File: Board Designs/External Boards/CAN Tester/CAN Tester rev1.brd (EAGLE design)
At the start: 83.8 x 100.3 mm, 27 parts, among them M1 Minifit, M2 Nanofit, M3 Nanofit-1, M4 Minifit-1, U1 ISOLATED CAN TRANSCIEVER, U3 TEENSY_3.2_SIMPLE, U4 CHARACTER_LCD

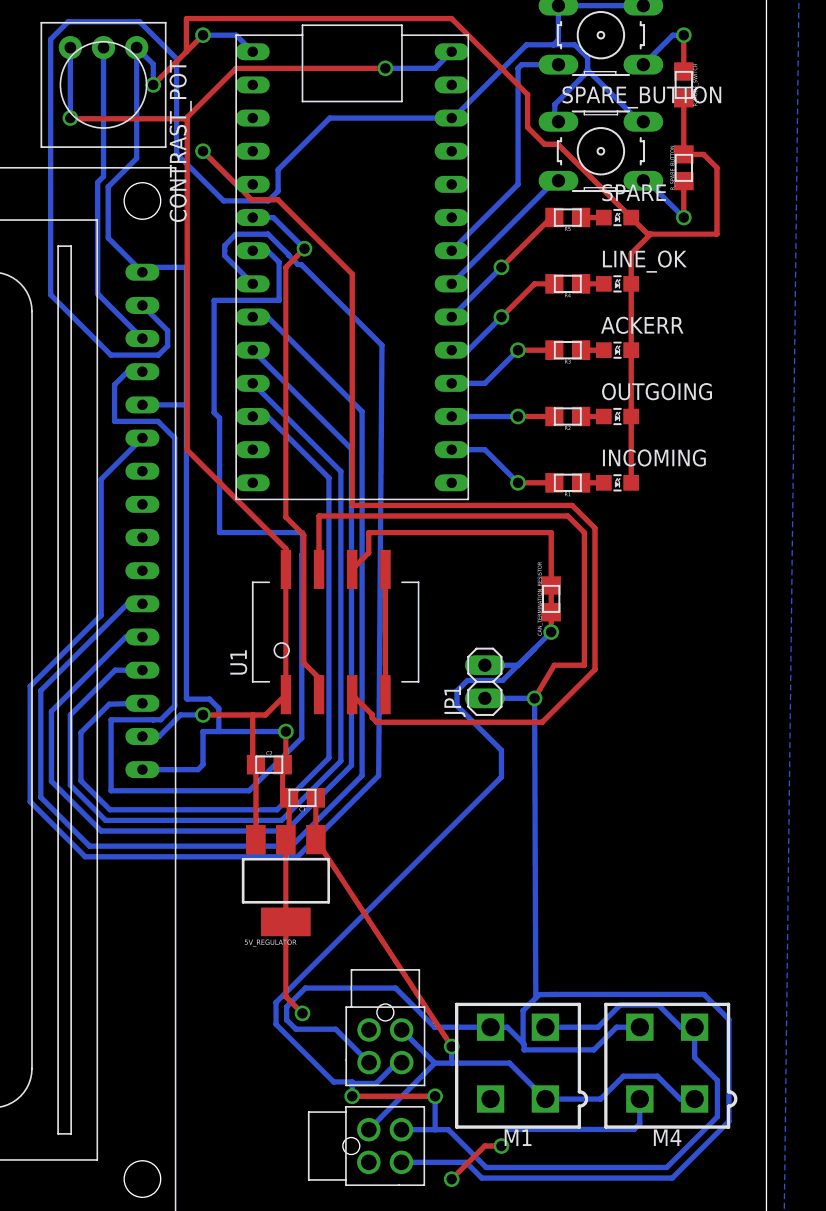
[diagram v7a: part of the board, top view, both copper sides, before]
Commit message: Finished CAN_Tester board
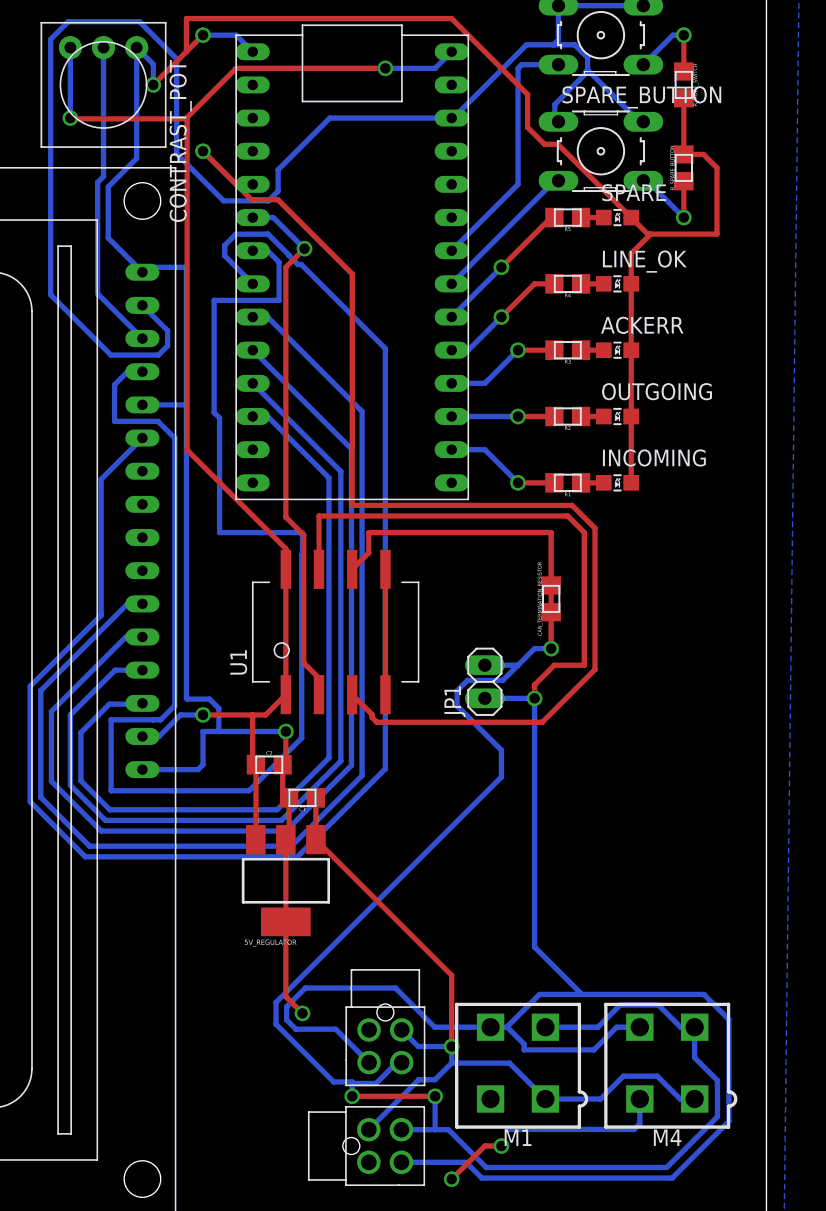
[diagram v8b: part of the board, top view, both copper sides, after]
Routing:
- net +12V: track 56.7 -> 58.6 mm
- net CANL: track 142.0 -> 141.0 mm
- net CANH: track 161.1 -> 161.8 mm
